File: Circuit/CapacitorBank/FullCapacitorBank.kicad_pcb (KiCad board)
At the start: 2 copper layers, 124.5 x 101.6 mm, 46 parts, among them J1 AC Power In, J2 Output+, J3 Output-, J4 To Voltage Sensing, J5 To Voltage Sensing, Q1 BT138-800, Q2 BT138-800, T1 6:75+75, U1 PC817, U2 PC817

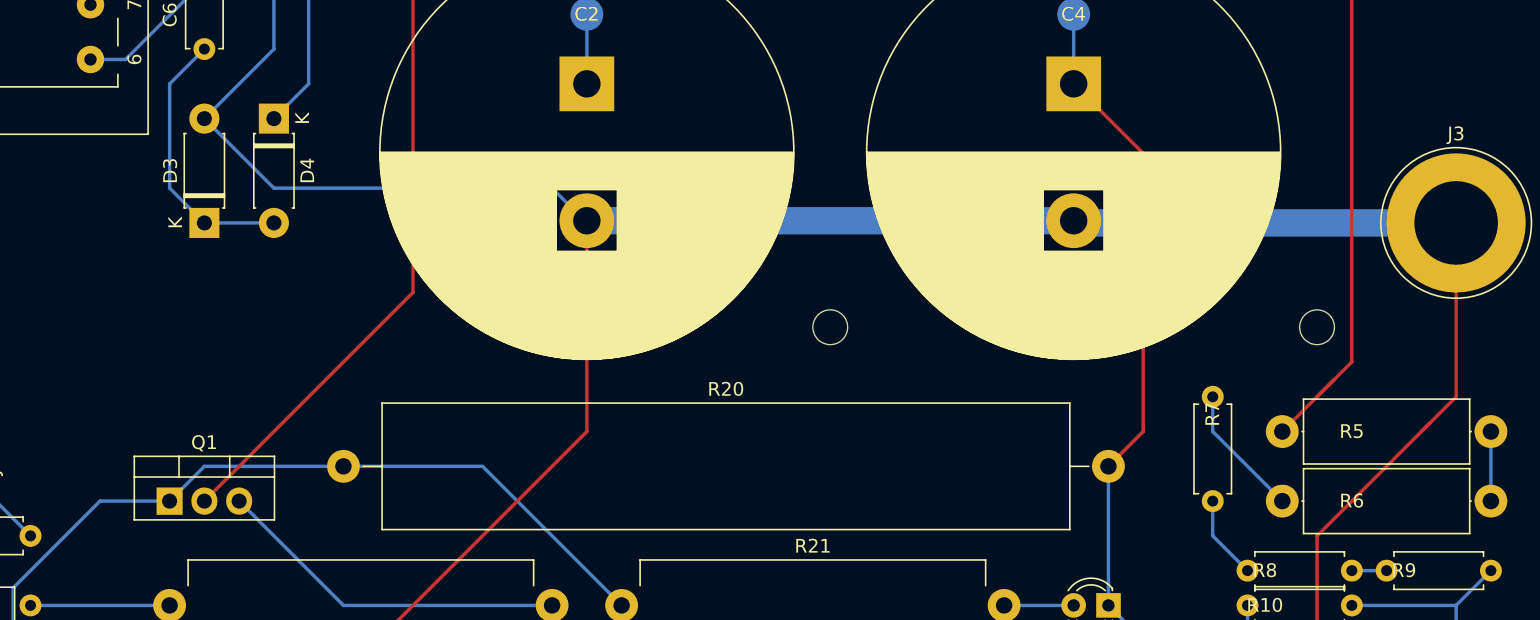
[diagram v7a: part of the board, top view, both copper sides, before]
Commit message: [Circuit] Enable to export gerber files
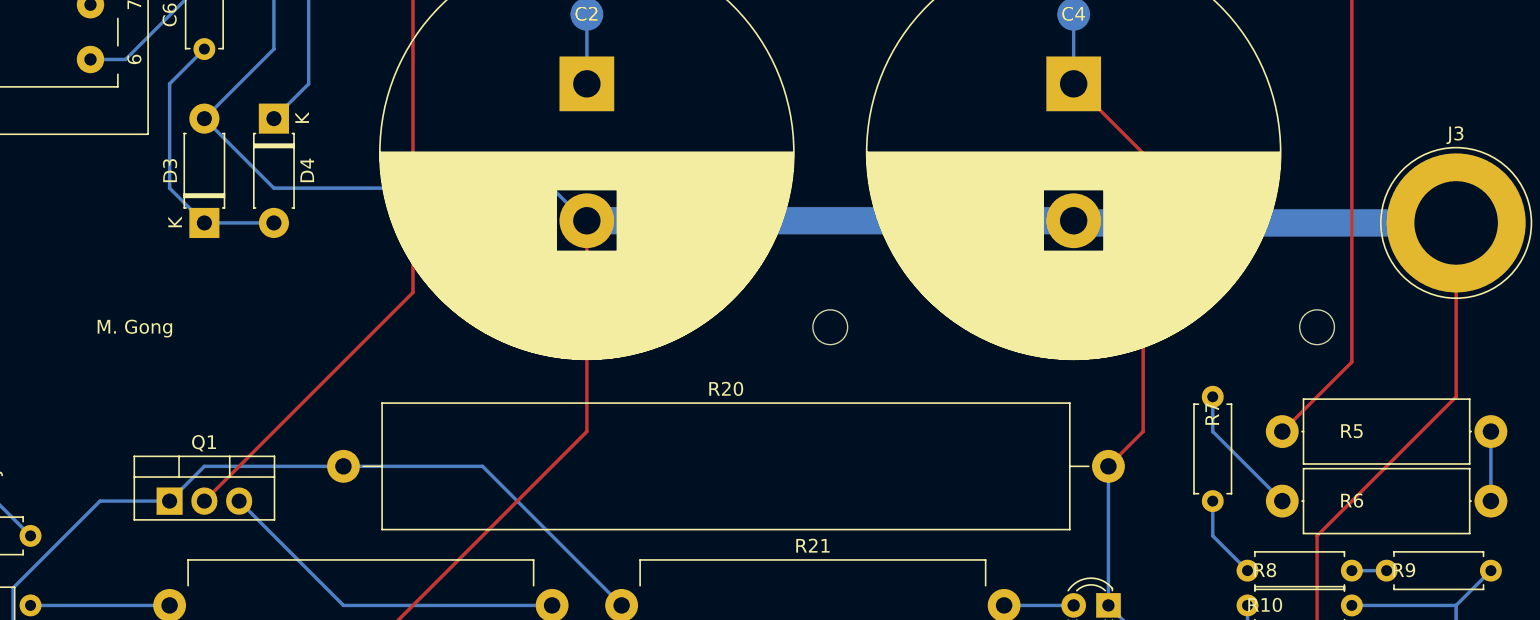
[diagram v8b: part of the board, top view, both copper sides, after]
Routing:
- net /PowerOut+: track 243.8 -> 242.0 mm
- net /PowerOut-: track 242.3 -> 241.5 mm
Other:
- board text added: "M. Gong"
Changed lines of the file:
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@@
   (general
     (thickness 1.6)
-    (drawings 19)
-    (tracks 133)
+    (drawings 20)
+    (tracks 129)
     (zones 0)
     (modules 46)
@@
       (creategerberjobfile false)
       (excludeedgelayer true)
-      (linewidth 0.100000)
+      (linewidth 0.250000)
       (plotframeref false)
       (viasonmask false)
@@
     )
   )
+  (gr_text "M. Gong" (at 63.5 91.44) (layer F.SilkS)
+    (effects (font (size 1 1) (thickness 0.15)))
+  )
   (gr_circle (center 165.1 114.3) (end 166.37 114.3) (layer Edge.Cuts) (width 0.05))
   (gr_circle (center 48.26 129.54) (end 49.53 129.54) (layer Edge.Cuts) (width 0.05))
@@
   (segment (start 68.58 104.14) (end 83.82 88.9) (width 0.25) (layer F.Cu) (net 1) (status 10))
   (segment (start 160.02 43.18) (end 152.4 50.8) (width 0.25) (layer F.Cu) (net 1) (status 10))
-  (segment (start 149.86 96.52) (end 152.4 93.98) (width 0.25) (layer F.Cu) (net 1))
-  (segment (start 149.86 96.52) (end 151.13 95.25) (width 0.25) (layer F.Cu) (net 1))
-  (segment (start 147.32 99.06) (end 149.86 96.52) (width 0.25) (layer F.Cu) (net 1) (status 10))
   (segment (start 73.66 50.8) (end 81.28 43.18) (width 0.25) (layer B.Cu) (net 1) (status 10))
   (segment (start 81.28 43.18) (end 96.52 43.18) (width 0.25) (layer B.Cu) (net 1) (status 20))
@@
   (segment (start 76.2 63.5) (end 76.2 73.66) (width 0.25) (layer B.Cu) (net 1))
   (segment (start 152.4 93.98) (end 152.4 50.8) (width 0.25) (layer F.Cu) (net 1))
-  (segment (start 73.66 50.8) (end 83.82 60.96) (width 0.25) (layer F.Cu) (net 1))
+  (segment (start 73.66 50.8) (end 83.82 60.96) (width 0.25) (layer F.Cu) (net 1) (status 10))
   (segment (start 83.82 88.9) (end 83.82 60.96) (width 0.25) (layer F.Cu) (net 1))
+  (segment (start 147.32 99.06) (end 152.4 93.98) (width 0.25) (layer F.Cu) (net 1) (status 10))
   (segment (start 132.24 83.82) (end 160.02 83.82) (width 2) (layer B.Cu) (net 2) (status 30))
   (segment (start 132.08 83.66) (end 96.52 83.66) (width 2) (layer B.Cu) (net 2) (status 30))
   (segment (start 96.36 83.82) (end 96.52 83.66) (width 0.25) (layer B.Cu) (net 2) (status 30))
-  (segment (start 149.86 127) (end 147.32 129.54) (width 0.25) (layer F.Cu) (net 2) (status 20))
-  (segment (start 149.86 106.68) (end 149.86 127) (width 0.25) (layer F.Cu) (net 2))
-  (segment (start 160.02 96.52) (end 158.115 98.425) (width 0.25) (layer F.Cu) (net 2))
-  (segment (start 158.115 98.425) (end 149.86 106.68) (width 0.25) (layer F.Cu) (net 2))
-  (segment (start 157.48 99.06) (end 158.115 98.425) (width 0.25) (layer F.Cu) (net 2))
   (segment (start 93.98 81.28) (end 96.52 83.82) (width 0.25) (layer B.Cu) (net 2) (status 20))
   (segment (start 68.58 76.2) (end 73.66 81.28) (width 0.25) (layer B.Cu) (net 2) (status 10))
@@
   (segment (start 71.5 63.88) (end 60.26 63.88) (width 0.25) (layer B.Cu) (net 2) (status 20))
   (segment (start 71.5 63.88) (end 71.5 53.72) (width 0.25) (layer B.Cu) (net 2))
-  (segment (start 160.02 96.52) (end 160.02 83.82) (width 0.25) (layer F.Cu) (net 2) (status 20))
+  (segment (start 160.02 83.82) (end 160.02 96.52) (width 0.25) (layer F.Cu) (net 2) (status 10))
+  (segment (start 160.02 96.52) (end 149.86 106.68) (width 0.25) (layer F.Cu) (net 2))
+  (segment (start 149.86 106.68) (end 149.86 127) (width 0.25) (layer F.Cu) (net 2))
+  (segment (start 149.86 127) (end 147.32 129.54) (width 0.25) (layer F.Cu) (net 2) (status 20))
   (segment (start 152.4 119.38) (end 154.94 119.38) (width 0.25) (layer B.Cu) (net 3) (status 30))
   (segment (start 152.4 119.38) (end 151.13 118.11) (width 0.25) (layer B.Cu) (net 3) (status 10))
@@
   (segment (start 137.16 114.3) (end 134.62 116.84) (width 0.25) (layer B.Cu) (net 12))
   (segment (start 134.62 116.84) (end 134.62 119.38) (width 0.25) (layer B.Cu) (net 12) (status 20))
-  (segment (start 137.16 78.74) (end 132.08 73.66) (width 0.25) (layer F.Cu) (net 12) (status 20))
-  (segment (start 134.62 101.6) (end 137.16 99.06) (width 0.25) (layer F.Cu) (net 12) (status 10))
-  (segment (start 137.16 99.06) (end 137.16 78.74) (width 0.25) (layer F.Cu) (net 12))
   (segment (start 144.78 114.3) (end 137.16 114.3) (width 0.25) (layer B.Cu) (net 12))
   (segment (start 144.78 114.3) (end 144.78 111.76) (width 0.25) (layer B.Cu) (net 12) (status 20))
+  (segment (start 132.08 73.66) (end 137.16 78.74) (width 0.25) (layer F.Cu) (net 12) (status 10))
+  (segment (start 137.16 78.74) (end 137.16 99.06) (width 0.25) (layer F.Cu) (net 12))
+  (segment (start 137.16 99.06) (end 134.62 101.6) (width 0.25) (layer F.Cu) (net 12) (status 20))
   (segment (start 68.58 60.96) (end 68.66 60.96) (width 0.25) (layer B.Cu) (net 13) (status 30))
   (segment (start 68.58 60.88) (end 68.5 60.88) (width 0.25) (layer B.Cu) (net 13) (status 30))
